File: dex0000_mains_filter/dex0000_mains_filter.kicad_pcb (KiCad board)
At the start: 2 copper layers, 75 x 71 mm, 16 parts, among them J1 Conn_01x03_Male, J2 Screw_Terminal_01x02

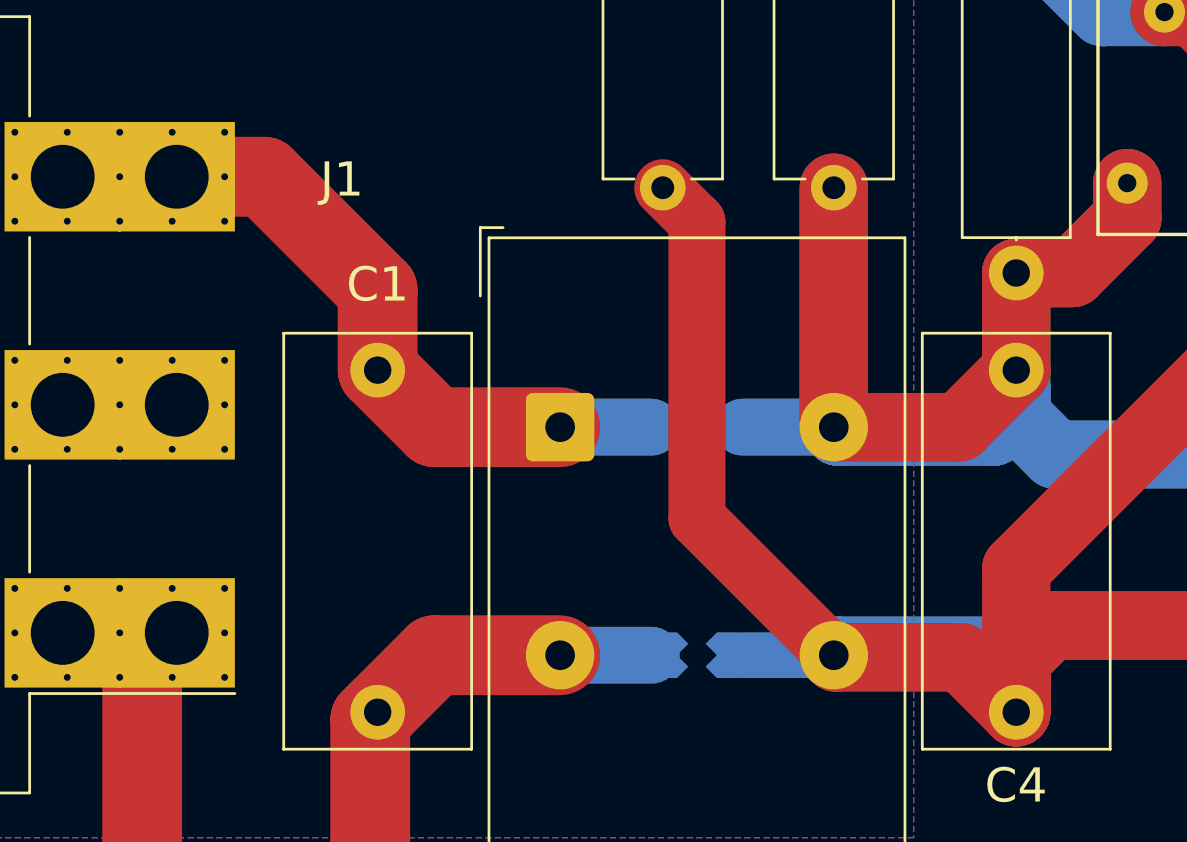
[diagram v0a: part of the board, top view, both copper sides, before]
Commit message: Add files via upload
updated design with documentation. Fixes 3.0mm self-clearances (now 0.75mm)
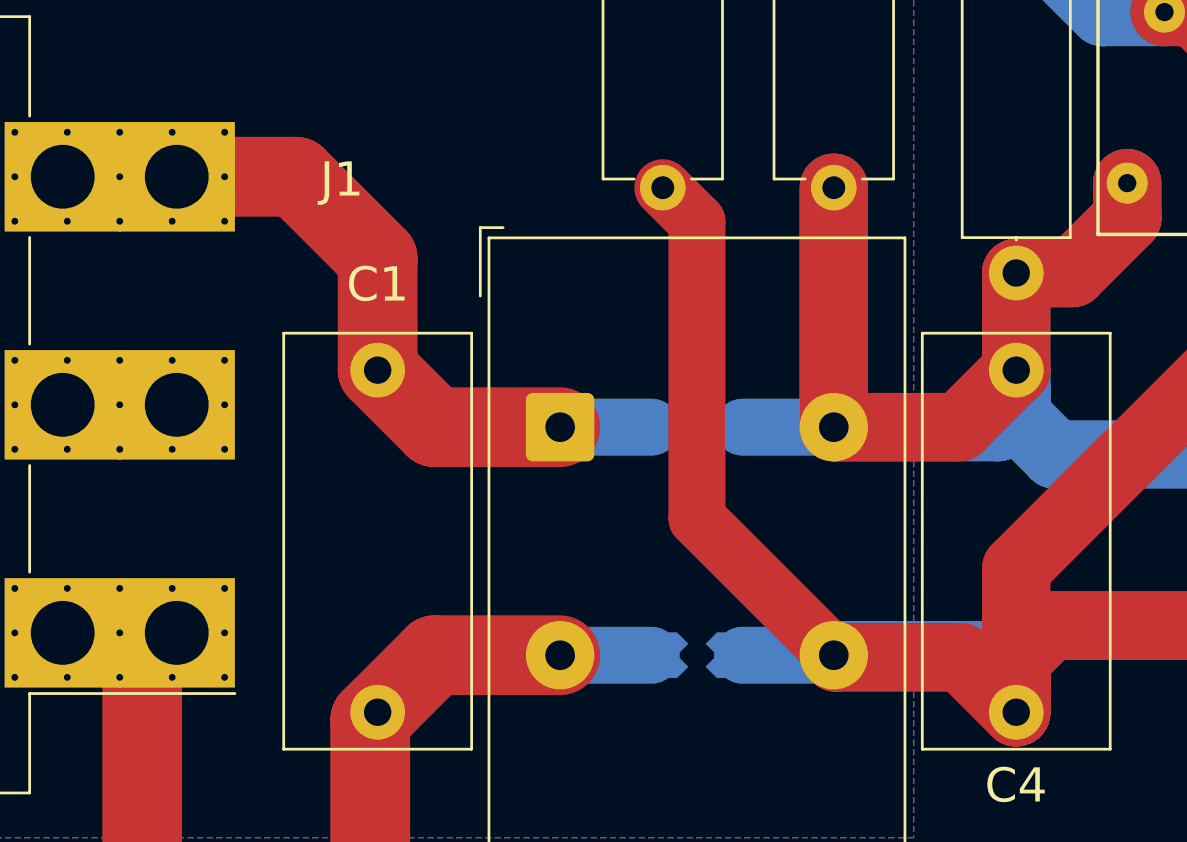
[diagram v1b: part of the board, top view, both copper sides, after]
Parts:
- J1: value Conn_01x03_Male -> 42820-3213
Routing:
- net /N: track 50.8 -> 52.5 mm
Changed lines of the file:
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@@
       (effects (font (size 1.5 1.5) (thickness 0.3)))
     )
-    (fp_text value "Conn_01x03_Male" (at 13.6 10.15 90) (layer "F.Fab")
-      (effects (font (size 1 1) (thickness 0.15)))
-    )
-    (fp_text user "${REFERENCE}" (at 16.42 10.65 90) (layer "F.Fab")
-      (effects (font (size 1.5 1.5) (thickness 0.3)))
+    (fp_text value "42820-3213" (at 13.6 10.15 90) (layer "F.Fab")
+      (effects (font (size 1 1) (thickness 0.15)))
     )
     (fp_line (start 7.81 -2.66) (end -2.81 -2.66) (layer "B.SilkS") (width 0.12))
@@
     (pad "3" thru_hole circle (at 7.1 18.05 180) (size 0.6 0.6) (drill 0.3) (layers *.Cu *.Mask)
       (net 4 "/N") (pinfunction "Pin_3"))
-    (model "${KISYS3DMOD}/Connector_Molex.3dshapes/Molex_Mini-Fit_Sr_42820-32XX_1x03_P10.00mm_Horizontal_ThermalVias.wrl"
+    (model "${KISYS3DMOD}/Connector_Molex.3dshapes/Molex_Mini-Fit_Sr_42820-32XX_1x03_P10.00mm_Horizontal_ThermalVias.wrl" hide
       (offset (xyz 0 0 0))
       (scale (xyz 1 1 1))
       (rotate (xyz 0 0 0))
+    )
+    (model "${KIPRJMOD}/../libs/Molex_Minifit_SR.pretty/3D/428203213.stp"
+      (offset (xyz 17.3 -10 6))
+      (scale (xyz 1 1 1))
+      (rotate (xyz -90 0 -90))
     )
   )
@@
       (effects (font (size 1 1) (thickness 0.15)))
     )
-    (fp_text user "${REFERENCE}" (at 3.8 -0.05 180) (layer "F.Fab")
+    (fp_text user "${REFERENCE}" (at 3.8 -0.05 180) (layer "F.Fab") hide
       (effects (font (size 1.5 1.5) (thickness 0.3)))
     )
@@
     (pad "2" thru_hole circle (at 7.5 0 90) (size 2.5 2.5) (drill 1.3) (layers *.Cu *.Mask)
       (net 6 "/N_OUT") (pinfunction "Pin_2"))
-    (model "${KISYS3DMOD}/TerminalBlock_MetzConnect.3dshapes/TerminalBlock_MetzConnect_Type171_RT13702HBWC_1x02_P7.50mm_Horizontal.wrl"
+    (model "${KISYS3DMOD}/TerminalBlock_MetzConnect.3dshapes/TerminalBlock_MetzConnect_Type171_RT13702HBWC_1x02_P7.50mm_Horizontal.wrl" hide
       (offset (xyz 0 0 0))
       (scale (xyz 1 1 1))
       (rotate (xyz 0 0 0))
+    )
+    (model "${KIPRJMOD}/../libs/PhoenixContact_GMKDS.pretty/3D/pxc_1731022_06_GMKDS-3-2_3D.stp"
+      (offset (xyz -3.75 -5.5 0))
+      (scale (xyz 1 1 1))
+      (rotate (xyz -90 0 90))
     )
   )
@@
   (segment (start 122.174324 99.802497) (end 122.174324 87.825676) (width 3) (layer "B.Cu") (net 3))
   (segment (start 130.5 85) (end 125 85) (width 3) (layer "B.Cu") (net 3))
-  (segment (start 117.52 64.02) (end 113.69 64.02) (width 3.5) (layer "F.Cu") (net 4))
-  (segment (start 122.5 72.5) (end 122.5 69) (width 3.5) (layer "F.Cu") (net 4))
   (segment (start 122.5 72.5) (end 125 75) (width 3.5) (layer "F.Cu") (net 4))
   (segment (start 125 75) (end 130.5 75) (width 3.5) (layer "F.Cu") (net 4))
-  (segment (start 122.5 69) (end 117.52 64.02) (width 3.5) (layer "F.Cu") (net 4))
-  (segment (start 122.5 72.5) (end 122.5 69) (width 3) (layer "B.Cu") (net 4))
-  (segment (start 122.5 69) (end 117.52 64.02) (width 3) (layer "B.Cu") (net 4))
+  (segment (start 122.5 72.5) (end 122.5 67.6) (width 3.5) (layer "F.Cu") (net 4))
+  (segment (start 118.92 64.02) (end 113.69 64.02) (width 3.5) (layer "F.Cu") (net 4))
+  (segment (start 122.5 67.6) (end 118.92 64.02) (width 3.5) (layer "F.Cu") (net 4))
+  (segment (start 118.92 64.02) (end 113.69 64.02) (width 3) (layer "B.Cu") (net 4))
   (segment (start 130.6 75) (end 134.5 75) (width 2.5) (layer "B.Cu") (net 4))
   (segment (start 130.6 75) (end 125 75) (width 3) (layer "B.Cu") (net 4))
-  (segment (start 117.52 64.02) (end 113.69 64.02) (width 3) (layer "B.Cu") (net 4))
+  (segment (start 122.5 67.6) (end 118.92 64.02) (width 3) (layer "B.Cu") (net 4))
+  (segment (start 122.5 72.5) (end 122.5 67.6) (width 3) (layer "B.Cu") (net 4))
   (segment (start 125 75) (end 122.5 72.5) (width 3) (layer "B.Cu") (net 4))
   (segment (start 158.3 56.8) (end 157 56.8) (width 3) (layer "F.Cu") (net 5))
@@
   (segment (start 152 83.7) (end 150.5 85.2) (width 3) (layer "B.Cu") (net 5))
   (segment (start 164.8 83.7) (end 152 83.7) (width 3) (layer "B.Cu") (net 5))
+  (segment (start 142.5 85) (end 138.5 85) (width 2.5) (layer "B.Cu") (net 5))
   (segment (start 150.5 85.7) (end 150.5 87.5) (width 3) (layer "B.Cu") (net 5))
-  (segment (start 142.5 85) (end 138.5 85) (width 2) (layer "B.Cu") (net 5))
-  (segment (start 142.7 84.8) (end 149.6 84.8) (width 3) (layer "B.Cu") (net 5))
   (segment (start 154.3 56.8) (end 150.5 53) (width 3) (layer "B.Cu") (net 5))
-  (segment (start 149.6 84.8) (end 150.5 85.7) (width 3) (layer "B.Cu") (net 5))
+  (segment (start 149.8 85) (end 150.5 85.7) (width 3) (layer "B.Cu") (net 5))
   (segment (start 150.5 85.2) (end 150.5 87.5) (width 3) (layer "B.Cu") (net 5))
-  (segment (start 142.5 85) (end 142.7 84.8) (width 3) (layer "B.Cu") (net 5))
+  (segment (start 142.5 85) (end 149.8 85) (width 3) (layer "B.Cu") (net 5))
   (segment (start 157 56.8) (end 154.3 56.8) (width 3) (layer "B.Cu") (net 5))
   (segment (start 150.5 72.5) (end 150.5 68.24) (width 3) (layer "F.Cu") (net 6))
@@
   (segment (start 148 75) (end 142.5 75) (width 3) (layer "F.Cu") (net 6))
   (segment (start 155.36667 65.83333) (end 155.36667 64.3) (width 3) (layer "F.Cu") (net 6))
-  (segment (start 142.7 75.2) (end 149.5 75.2) (width 3) (layer "B.Cu") (net 6))
   (segment (start 150.5 72.5) (end 150.5 68.24) (width 3) (layer "B.Cu") (net 6))
   (segment (start 142.5 75) (end 138.5 75) (width 2.5) (layer "B.Cu") (net 6))
-  (segment (start 149.5 75.2) (end 150.5 74.2) (width 3) (layer "B.Cu") (net 6))
+  (segment (start 150.5 74.2) (end 150.5 73.3) (width 3) (layer "B.Cu") (net 6))
+  (segment (start 149.7 75) (end 150.5 74.2) (width 3) (layer "B.Cu") (net 6))
   (segment (start 142.5 75) (end 142.5 64.5) (width 3) (layer "B.Cu") (net 6))
-  (segment (start 150.5 74.2) (end 150.5 73.3) (width 3) (layer "B.Cu") (net 6))
   (segment (start 150.5 73.3) (end 150.5 72.5) (width 3) (layer "B.Cu") (net 6))
   (segment (start 164.8 76.2) (end 152.2 76.2) (width 3) (layer "B.Cu") (net 6))
+  (segment (start 142.5 75) (end 149.7 75) (width 3) (layer "B.Cu") (net 6))
   (segment (start 152.2 76.2) (end 150.5 74.5) (width 3) (layer "B.Cu") (net 6))
   (segment (start 155.36667 65.83333) (end 152.96 68.24) (width 3) (layer "B.Cu") (net 6))
   (segment (start 152.96 68.24) (end 150.5 68.24) (width 3) (layer "B.Cu") (net 6))
-  (segment (start 142.5 75) (end 142.7 75.2) (width 3) (layer "B.Cu") (net 6))
   (segment (start 155.36667 64.3) (end 155.36667 65.83333) (width 3) (layer "B.Cu") (net 6))
   (segment (start 150.5 74.5) (end 150.5 73.3) (width 3) (layer "B.Cu") (net 6))
